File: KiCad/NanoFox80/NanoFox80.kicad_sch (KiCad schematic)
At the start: 53 parts, among them J101 Conn_01x02, J102 Conn_01x02, J111 DB9 Female, J112 Conn_01x02, J113 Conn_01x02, J115 Conn_01x02, P101 ISP/PDI, Q101 BSS84W-7-F, Q102 BSS138W-7-F, SW101 SW_SPST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

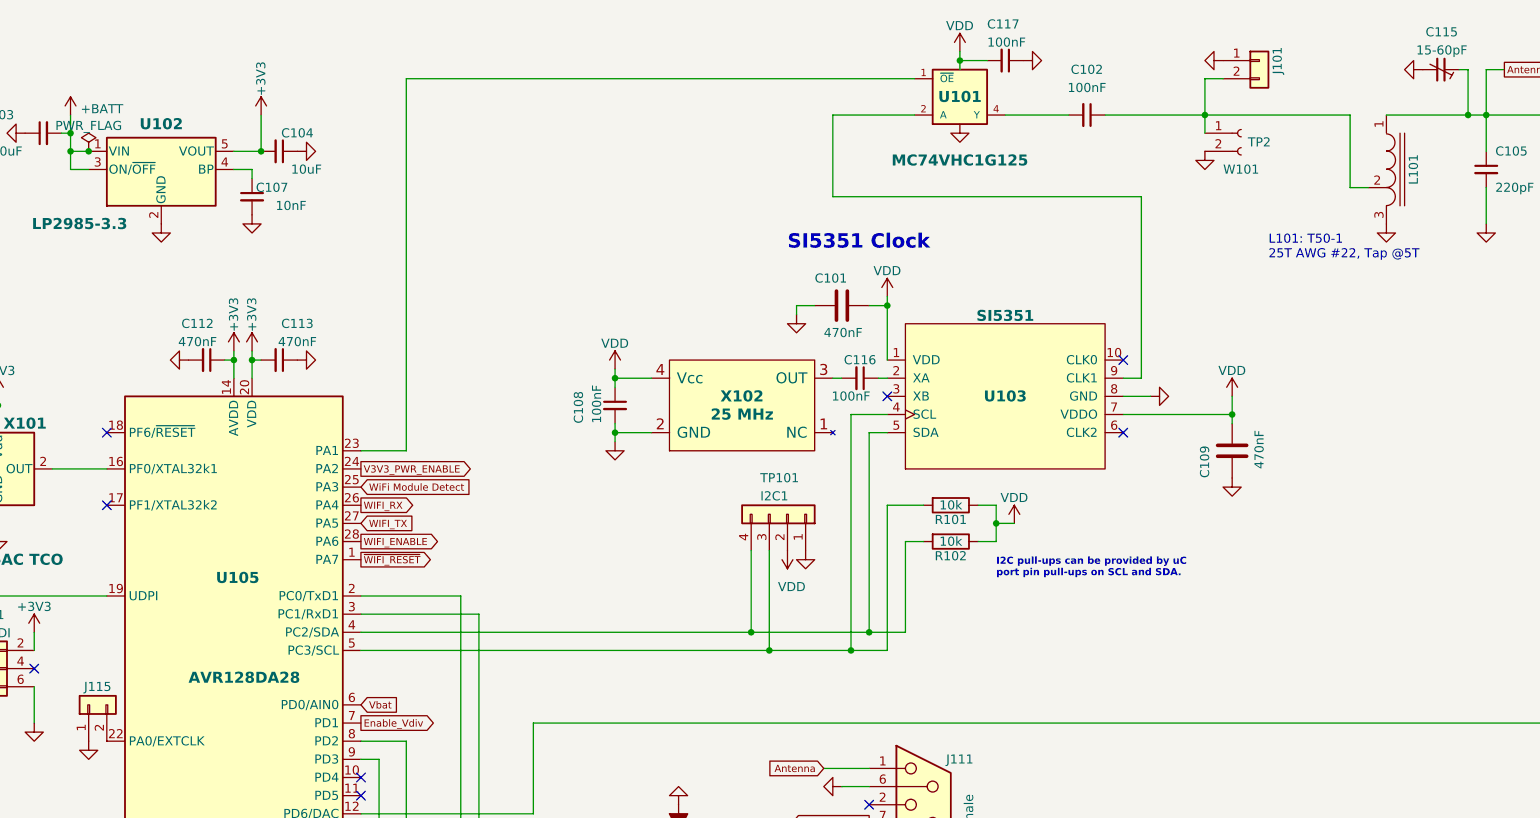
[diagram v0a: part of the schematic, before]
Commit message: Schematic Updates
o Corrected the device symbol for the microcontroller.
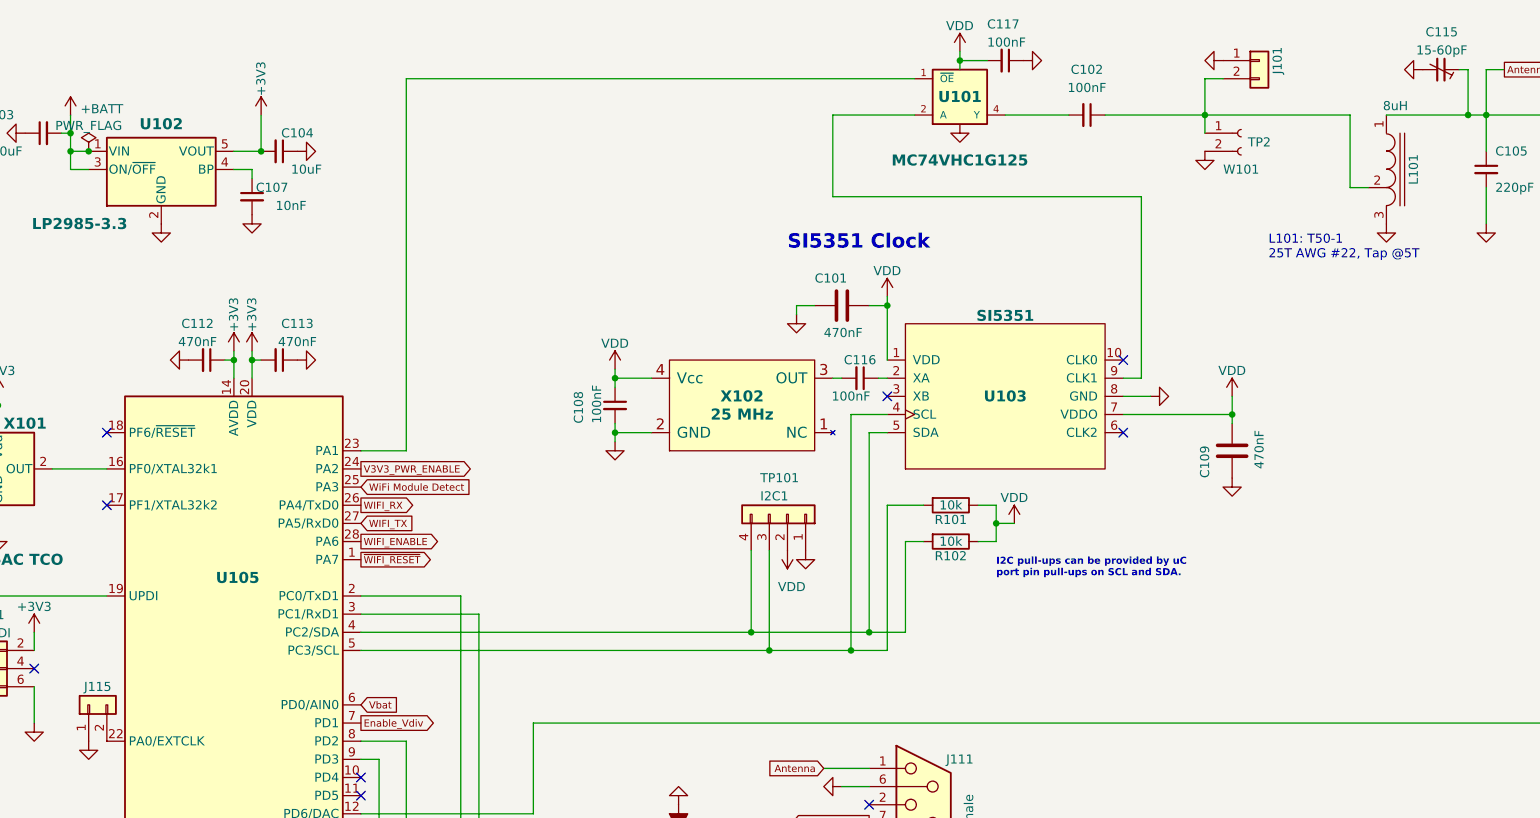
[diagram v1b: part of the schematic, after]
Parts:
- L101: value (none) -> 8uH; footprint (none) -> Transformer_THT:Autotransformer_Toroid_1Tap_Horizontal_D14.0mm_Amidon-T50
- U105: value AVR128DA28 -> (none)
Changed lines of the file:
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@@
     (in_bom yes) (on_board yes)
     (property "Reference" "L101" (id 0) (at 224.79 36.83 90))
-    (property "Value" "" (id 1) (at 222.25 27.94 0))
-    (property "Footprint" "" (id 2) (at 222.25 52.07 0)
+    (property "Value" "8uH" (id 1) (at 222.25 27.94 0))
+    (property "Footprint" "Transformer_THT:Autotransformer_Toroid_1Tap_Horizontal_D14.0mm_Amidon-T50" (id 2) (at 222.25 52.07 0)
       (effects (font (size 1.27 1.27)) hide)
     )
@@
       (effects (font (size 1.54 1.54) bold) (justify left))
     )
-    (property "Value" "AVR128DA28" (id 1) (at 53.34 107.95 0)
+    (property "Value" "" (id 1) (at 53.34 107.95 0)
       (effects (font (size 1.54 1.54) bold) (justify left))
     )

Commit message: KiCad
o Schematic updates
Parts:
- removed C106: 470nF, Capacitor_SMD:C_0805_2012Metric_Pad1.18x1.45mm_HandSolder, symbol Device:C_Small
- removed D102: SMV1253-079LF, Diode_SMD:D_SC-80, symbol Device:D_Capacitance_Filled
- removed FB101: FerriteBead_Small, Inductor_SMD:Ferrite_Bead_NFZ32BW881_Reflow, symbol Device:FerriteBead_Small
- added C?: 15-60pF, Capacitor_THT:CP_Radial_Ceramic_Trimmer_D9.4mm_P8.00mm, symbol Device:C_Trim_Small
- added D?: 4.7V, symbol Device:D_Zener_Small_Filled
- added J?: Conn_01x02, Connector_PinSocket_2.54mm:PinSocket_1x02_P2.54mm_Vertical, symbol Connector_Generic:Conn_01x02
- added JP?: (no value), symbol Jumper:SolderJumper_3_Bridged12
- U105: value (none) -> AVR128DA28
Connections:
- net Antenna: now also C?.2
- net GND: now also C?.1, D?.2 (A), J?.1 (Pin_1), JP?.1 (A)
- net at U105.12 (PD6/DAC): now also J?.2 (Pin_2)
- net at U101.1 (~{OE}): now also JP?.2 (C); no longer U105.23 (PA1)
- net at C102.2, U101.4 (Y): now also D?.1 (K)
- new net: JP?.3 (B), U105.23 (PA1)
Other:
- note removed: "8-69pF"

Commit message: Update NanoFox80.kicad_sch
Rev A proposed changes
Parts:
- removed C?: 15-60pF, Capacitor_THT:CP_Radial_Ceramic_Trimmer_D9.4mm_P8.00mm, symbol Device:C_Trim_Small
- removed JP?: (no value), symbol Jumper:SolderJumper_3_Bridged12
- removed R108: 1k, Resistor_SMD:R_0805_2012Metric_Pad1.20x1.40mm_HandSolder, symbol Device:R
- removed R109: 100k, Resistor_SMD:R_0805_2012Metric_Pad1.20x1.40mm_HandSolder, symbol Device:R
- removed R110: 162k, Resistor_SMD:R_0805_2012Metric_Pad1.20x1.40mm_HandSolder, symbol Device:R
- removed R111: 12.4k, Resistor_SMD:R_0805_2012Metric_Pad1.20x1.40mm_HandSolder, symbol Device:R
- removed U101: MC74VHC1G125, Package_TO_SOT_SMD:TSOT-23-5, symbol 74xx:MC74VHC1G125
- removed W101: TP2, Measurement:Measurement_Point_ScopeProbe_Round-SMD-2sides-Pad_Small, symbol Connector:Conn_01x02_Female
- removed W102: TP3, Measurement:Measurement_Point_ScopeProbe_Round-SMD-2sides-Pad_Small, symbol Connector:Conn_01x02_Female
- added C106: 15-60pF, Capacitor_THT:CP_Radial_Ceramic_Trimmer_D9.4mm_P8.00mm, symbol Device:C_Trim_Small
- added C118, C119: (no value), Capacitor_SMD:C_0805_2012Metric, symbol Device:C_Small
- added D105: (no value), Diode_SMD:D_SOD-523, symbol Diode:1N914WT
- added D106: LED_Filled, LED_SMD:LED_APDA1806SECK, symbol Device:LED_Filled
- added J104: Conn_01x02, Connector_PinSocket_2.54mm:PinSocket_1x02_P2.54mm_Vertical, symbol Connector_Generic:Conn_01x02
- added L102: (no value), symbol pspice:INDUCTOR
- added Q103: (no value), symbol Transistor_BJT:DTC113Z
- added R103, R108, R109, R110, R111: (no value), symbol Device:R_Small_US
- gave numbers to parts that had none: 2
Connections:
- net +BATT: now also Q101.3 (D), R110.2; no longer BT101.2 (+), Q101.2 (S)
- net Antenna: now also L102.1; no longer AE101.2 (A), J102.2 (Pin_2)
- net GND: now also C106.1, C118.2, C119.2, D106.1 (K), J104.1 (Pin_1), R111.1
- net Vbat: now also R110.1, R111.2
- net at Q101.1 (G), Q102.3 (D): now also J112.2 (Pin_2), SW101.1 (A), D105.1 (K), R109.2
- net at U103.9 (CLK1): now also Q103.1 (B)
- net at J101.2 (Pin_2), L101.2 (TAP): now also C106.2, C118.1, R103.2; no longer C102.1
- net at D101.2 (A), J113.2 (Pin_2): now also R108.1
- net at U105.8 (PD2): now also R108.2
- net at C102.2: now also C119.1, L102.2; no longer D102.1 (K)
- net at U105.10 (PD4): now also D106.2 (A), J104.2 (Pin_2)
- net VCC renamed VDD
- net VDD: now also Q103.3 (C)
- new net: BT101.2 (+), Q101.2 (S), R109.1
- new net: D105.2 (A), U105.9 (PD3)
- new net: D102.1 (K), Q103.2 (E), R103.1
- new net: AE101.2 (A), C102.1, J102.2 (Pin_2)
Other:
- note added: "GREEN"
- note added: "RED"
- moved on the sheet: AE101, BT101, C101, C102, C105, C108, C109, C110, C111, C114, C115, C116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

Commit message: +BATT Fix
Schematic change
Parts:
- C118, C119: value (none) -> TBD pF
- D105: value (none) -> 1N914WT
- L102: value (none) -> TBD nF
- Q103: value (none) -> DTC113Z
- R103: value (none) -> 10
- R108: value (none) -> 1k
- R109: value (none) -> 100k
- R110: value (none) -> 162k
- R111: value (none) -> 12.4k
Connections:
- net +BATT: now also BT101.2 (+), Q101.2 (S), R109.1; no longer C103.2, C110.2, Q101.3 (D), R110.2, U102.1 (VIN), U102.3 (ON/~{OFF}), U104.1 (VIN)
- new net +VSW: C103.2, C110.2, Q101.3 (D), R110.2, U102.1 (VIN), U102.3 (ON/~{OFF}), U104.1 (VIN)
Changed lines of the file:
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@@
   (junction (at 137.16 55.88) (diameter 0) (color 0 0 0 0)
   )
-  (junction (at 50.8 158.75) (diameter 0) (color 0 0 0 0)
-  )
   (junction (at 116.84 182.88) (diameter 0) (color 0 0 0 0)
   )
@@
   (junction (at 26.67 69.85) (diameter 0) (color 0 0 0 0)
   )
+  (junction (at 50.8 158.75) (diameter 0) (color 0 0 0 0)
+  )
   (junction (at 88.9 151.13) (diameter 0) (color 0 0 0 0)
   )
@@
   (junction (at 73.66 151.13) (diameter 0) (color 0 0 0 0)
   )
+  (junction (at 31.75 151.13) (diameter 0) (color 0 0 0 0)
+  )
   (junction (at 121.92 138.43) (diameter 0) (color 0 0 0 0)
   )
@@
     (stroke (width 0) (type default) (color 0 0 0 0))
   )
-  (wire (pts (xy 50.8 158.75) (xy 53.34 158.75))
-    (stroke (width 0) (type default) (color 0 0 0 0))
-  )
   (wire (pts (xy 41.91 151.13) (xy 73.66 151.13))
     (stroke (width 0) (type default) (color 0 0 0 0))
@@
     (in_bom yes) (on_board yes) (fields_autoplaced)
     (property "Reference" "L102" (id 0) (at 250.19 44.6872 0))
-    (property "Value" "" (id 1) (at 250.19 47.2241 0))
+    (property "Value" "TBD nF" (id 1) (at 250.19 47.2241 0))
     (property "Footprint" "" (id 2) (at 250.19 49.53 0)
       (effects (font (size 1.27 1.27)) hide)
@@
     (in_bom yes) (on_board yes)
     (property "Reference" "R109" (id 0) (at 36.83 148.59 90))
-    (property "Value" "" (id 1) (at 36.83 153.67 90))
+    (property "Value" "100k" (id 1) (at 36.83 153.67 90))
     (property "Footprint" "" (id 2) (at 36.83 151.13 0)
       (effects (font (size 1.27 1.27)) hide)
@@
     (pin "1")
   )
+  (symbol (lib_id "power:+VSW") (at 50.8 158.75 0) (unit 1)
+    (in_bom yes) (on_board yes) (fields_autoplaced)
+    (property "Reference" "#PWR?" (id 0) (at 50.8 162.56 0)
+      (effects (font (size 1.27 1.27)) hide)
+    )
+    (property "Value" "+VSW" (id 1) (at 50.8 155.1742 0))
+    (property "Footprint" "" (id 2) (at 50.8 158.75 0)
+      (effects (font (size 1.27 1.27)) hide)
+    )
+    (property "Datasheet" "" (id 3) (at 50.8 158.75 0)
+      (effects (font (size 1.27 1.27)) hide)
+    )
+    (pin "1")
+  )
   (symbol (lib_id "power:+3V3") (at 26.67 68.58 0) (unit 1)
     (in_bom yes) (on_board yes) (fields_autoplaced)
@@
       (effects (font (size 1.27 1.27)) (justify left))
     )
-    (property "Value" "" (id 1) (at 252.73 58.42 0)
+    (property "Value" "TBD pF" (id 1) (at 252.73 58.42 0)
       (effects (font (size 1.27 1.27)) (justify left))
     )
@@
       (effects (font (size 1.27 1.27)) (justify right))
     )
-    (property "Value" "" (id 1) (at 69.85 146.05 90)
+    (property "Value" "1N914WT" (id 1) (at 69.85 146.05 90)
       (effects (font (size 1.27 1.27)) (justify right))
     )
@@
     (pin "5")
   )
-  (symbol (lib_id "power:+BATT") (at 36.83 29.21 0) (unit 1)
-    (in_bom yes) (on_board yes) (fields_autoplaced)
-    (property "Reference" "#PWR0104" (id 0) (at 36.83 33.02 0)
-      (effects (font (size 1.27 1.27)) hide)
-    )
-    (property "Value" "+BATT" (id 1) (at 38.227 28.3738 0)
-      (effects (font (size 1.27 1.27)) (justify left))
-    )
-    (property "Footprint" "" (id 2) (at 36.83 29.21 0)
-      (effects (font (size 1.27 1.27)) hide)
-    )
-    (property "Datasheet" "" (id 3) (at 36.83 29.21 0)
-      (effects (font (size 1.27 1.27)) hide)
-    )
-    (pin "1")
-  )
   (symbol (lib_id "power:VDD") (at 154.94 86.36 0) (unit 1)
     (in_bom yes) (on_board yes) (fields_autoplaced)
@@
       (effects (font (size 1.27 1.27)) (justify left))
     )
-    (property "Value" "" (id 1) (at 186.182 38.5322 0)
+    (property "Value" "DTC113Z" (id 1) (at 186.182 38.5322 0)
       (effects (font (size 1.27 1.27)) (justify left))
     )
@@
     (pin "1")
   )
-  (symbol (lib_id "power:+BATT") (at 53.34 158.75 270) (unit 1)
+  (symbol (lib_id "power:+BATT") (at 31.75 151.13 0) (unit 1)
     (in_bom yes) (on_board yes) (fields_autoplaced)
-    (property "Reference" "#PWR0154" (id 0) (at 49.53 158.75 0)
+    (property "Reference" "#PWR0154" (id 0) (at 31.75 154.94 0)
       (effects (font (size 1.27 1.27)) hide)
     )
-    (property "Value" "+BATT" (id 1) (at 56.515 159.1838 90)
-      (effects (font (size 1.27 1.27)) (justify left))
-    )
-    (property "Footprint" "" (id 2) (at 53.34 158.75 0)
+    (property "Value" "+BATT" (id 1) (at 31.75 147.5542 0))
+    (property "Footprint" "" (id 2) (at 31.75 151.13 0)
       (effects (font (size 1.27 1.27)) hide)
     )
-    (property "Datasheet" "" (id 3) (at 53.34 158.75 0)
+    (property "Datasheet" "" (id 3) (at 31.75 151.13 0)
       (effects (font (size 1.27 1.27)) hide)
     )
@@
     (pin "2")
   )
+  (symbol (lib_id "power:+VSW") (at 90.17 177.8 0) (unit 1)
+    (in_bom yes) (on_board yes) (fields_autoplaced)
+    (property "Reference" "#PWR?" (id 0) (at 90.17 181.61 0)
+      (effects (font (size 1.27 1.27)) hide)
+    )
+    (property "Value" "" (id 1) (at 90.17 174.2242 0))
+    (property "Footprint" "" (id 2) (at 90.17 177.8 0)
+      (effects (font (size 1.27 1.27)) hide)
+    )
+    (property "Datasheet" "" (id 3) (at 90.17 177.8 0)
+      (effects (font (size 1.27 1.27)) hide)
+    )
+    (pin "1")
+  )
   (symbol (lib_id "power:GND") (at 31.75 114.3 0) (unit 1)
     (in_bom yes) (on_board yes) (fields_autoplaced)
@@
     (pin "2")
   )
+  (symbol (lib_id "power:+VSW") (at 36.83 29.21 0) (unit 1)
+    (in_bom yes) (on_board yes) (fields_autoplaced)
+    (property "Reference" "#PWR?" (id 0) (at 36.83 33.02 0)
+      (effects (font (size 1.27 1.27)) hide)
+    )
+    (property "Value" "+VSW" (id 1) (at 36.83 25.6342 0))
+    (property "Footprint" "" (id 2) (at 36.83 29.21 0)
+      (effects (font (size 1.27 1.27)) hide)
+    )
+    (property "Datasheet" "" (id 3) (at 36.83 29.21 0)
+      (effects (font (size 1.27 1.27)) hide)
+    )
+    (pin "1")
+  )
   (symbol (lib_id "power:+BATT") (at 146.05 176.53 0) (unit 1)
     (in_bom yes) (on_board yes) (fields_autoplaced)
@@
     (in_bom yes) (on_board yes) (fields_autoplaced)
     (property "Reference" "R103" (id 0) (at 191.77 44.9412 90))
-    (property "Value" "" (id 1) (at 191.77 47.4781 90))
+    (property "Value" "10" (id 1) (at 191.77 47.4781 90))
     (property "Footprint" "" (id 2) (at 191.77 49.53 0)
       (effects (font (size 1.27 1.27)) hide)
@@
     (in_bom yes) (on_board yes)
     (property "Reference" "R108" (id 0) (at 81.28 132.08 90))
-    (property "Value" "" (id 1) (at 86.36 132.08 90))
+    (property "Value" "1k" (id 1) (at 86.36 132.08 90))
     (property "Footprint" "" (id 2) (at 83.82 132.08 0)
       (effects (font (size 1.27 1.27)) hide)
@@
     (in_bom yes) (on_board yes)
     (property "Reference" "R111" (id 0) (at 48.26 180.34 90))
-    (property "Value" "" (id 1) (at 53.34 180.34 90))
+    (property "Value" "12.4k" (id 1) (at 53.34 180.34 90))
     (property "Footprint" "" (id 2) (at 50.8 180.34 0)
       (effects (font (size 1.27 1.27)) hide)
@@
       (effects (font (size 1.27 1.27)) (justify left))
     )
-    (property "Value" "" (id 1) (at 213.36 58.42 0)
+    (property "Value" "TBD pF" (id 1) (at 213.36 58.42 0)
       (effects (font (size 1.27 1.27)) (justify left))
     )
@@
     (in_bom yes) (on_board yes)
     (property "Reference" "R110" (id 0) (at 48.26 170.18 90))
-    (property "Value" "" (id 1) (at 53.34 170.18 90))
+    (property "Value" "162k" (id 1) (at 53.34 170.18 90))
     (property "Footprint" "" (id 2) (at 50.8 170.18 0)
       (effects (font (size 1.27 1.27)) hide)
@@
     (pin "1")
   )
-  (symbol (lib_id "power:+BATT") (at 90.17 177.8 0) (unit 1)
-    (in_bom yes) (on_board yes) (fields_autoplaced)
-    (property "Reference" "#PWR0128" (id 0) (at 90.17 181.61 0)
-      (effects (font (size 1.27 1.27)) hide)
-    )
-    (property "Value" "+BATT" (id 1) (at 91.567 176.9638 0)
-      (effects (font (size 1.27 1.27)) (justify left))
-    )
-    (property "Footprint" "" (id 2) (at 90.17 177.8 0)
-      (effects (font (size 1.27 1.27)) hide)
-    )
-    (property "Datasheet" "" (id 3) (at 90.17 177.8 0)
-      (effects (font (size 1.27 1.27)) hide)
-    )
-    (pin "1")
-  )
   (symbol (lib_id "MCU_Microchip_AVR:AVR128DA28") (at 59.69 101.6 0) (unit 1)
     (in_bom yes) (on_board yes)
@@
       (reference "#PWR0103") (unit 1) (value "GND") (footprint "")
     )
-    (path "/73c30ded-2dd8-4aab-8591-6bf32d308f5d"
-      (reference "#PWR0104") (unit 1) (value "+BATT") (footprint "")
-    )
     (path "/c932b361-059f-4797-bb48-55acd54d22ae"
       (reference "#PWR0105") (unit 1) (value "+3V3") (footprint "")
@@
       (reference "#PWR0127") (unit 1) (value "GND") (footprint "")
     )
-    (path "/f2ddb6c9-442a-4176-8a32-fe9e59c11904"
-      (reference "#PWR0128") (unit 1) (value "+BATT") (footprint "")
-    )
     (path "/4f7a1eba-8dbc-4c27-9d23-77ce339ae68b"
       (reference "#PWR0129") (unit 1) (value "VDD") (footprint "")
@@
       (reference "#PWR0202") (unit 1) (value "GND") (footprint "")
     )
-    (path "/a6cf679a-8fe8-43b4-a04f-10097436e2b4/61cfe4c0-62bf-4283-bd63-b0003d403127"
-      (reference "#PWR0203") (unit 1) (value "+BATT") (footprint "")
-    )
     (path "/a6cf679a-8fe8-43b4-a04f-10097436e2b4/02034456-d704-450b-856e-6d640ab38367"
       (reference "#PWR0204") (unit 1) (value "GND") (footprint "")
@@
       (reference "#PWR0209") (unit 1) (value "GND") (footprint "")
     )
+    (path "/402b505a-3134-4180-8252-3cb6368585af"
+      (reference "#PWR?") (unit 1) (value "+VSW") (footprint "")
+    )
+    (path "/a6cf679a-8fe8-43b4-a04f-10097436e2b4/6fe5f251-d125-403e-ab6b-dbe26cac51a9"
+      (reference "#PWR?") (unit 1) (value "+VSW") (footprint "")
+    )
+    (path "/a3e4e30c-206c-441f-ab18-6136621c1881"
+      (reference "#PWR?") (unit 1) (value "+VSW") (footprint "")
+    )
+    (path "/bd6b6d07-bcc0-4e70-87e3-edf6a5aca5a3"
+      (reference "#PWR?") (unit 1) (value "+VSW") (footprint "")
+    )
     (path "/c938e709-b8e6-465b-a1ac-8390c5f3f4c9"
